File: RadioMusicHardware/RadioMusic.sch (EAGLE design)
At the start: 23 parts, among them IC1 TL074P, IC2 7805L, U1 USD-SOCKETNEW

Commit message: Output circuitry
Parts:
- added C3, C6: 1n, TomW:C-EU050-024X044
- added C7, C8: 100n, TomW:C-EU050-025X075
- added R3, R5, R6: 8.2k, TomW:R-EU_STANDARD_RESISTOR
- added R4: 220R, TomW:R-EU_STANDARD_RESISTOR
- added R7: 1k, TomW:R-EU_STANDARD_RESISTOR
- added R8: 3.3K, TomW:R-EU_STANDARD_RESISTOR
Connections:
- new net DAC: C8.2, U$1.RESET
- new net N$10: C8.1, R5.1
- new net N$2: C6.1, IC1C.+IN, R3.2
- new net N$4: C3.2, R3.1, R5.2
- new net N$5: C3.1, C7.2, IC1C.-IN, IC1C.OUT
- new net N$6: C7.1, IC1D.+IN, R6.2
- new net N$7: IC1D.-IN, R7.2, R8.1
- new net N$8: IC1D.OUT, R4.1, R8.2
- new net N$9: OUT1.3, R4.2
- net GND: now also C6.2, OUT1.5, R6.1, R7.1
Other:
- note added: "NB Outline is for Teensy3 Teensy3.1 has DAC output where Reset was on Teensy3"
- moved on the sheet: IC1C, IC1D, OUT1, OUT2, U1
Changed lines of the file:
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@@
 <layer number="97" name="Info" color="7" fill="1" visible="yes" active="yes"/>
 <layer number="98" name="Guide" color="6" fill="1" visible="yes" active="yes"/>
+<layer number="99" name="SpiceOrder" color="5" fill="1" visible="yes" active="yes"/>
 <layer number="100" name="Muster" color="7" fill="1" visible="no" active="no"/>
 <layer number="101" name="Patch_Top" color="12" fill="4" visible="yes" active="yes"/>
@@
 <part name="SUPPLY3" library="supply2" deviceset="GND" device=""/>
 <part name="SUPPLY4" library="supply2" deviceset="GND" device=""/>
+<part name="SUPPLY5" library="supply2" deviceset="GND" device=""/>
+<part name="R3" library="TomW" deviceset="R-EU_" device="STANDARD_RESISTOR" value="8.2k"/>
+<part name="R4" library="TomW" deviceset="R-EU_" device="STANDARD_RESISTOR" value="220R"/>
+<part name="R5" library="TomW" deviceset="R-EU_" device="STANDARD_RESISTOR" value="8.2k"/>
+<part name="C3" library="TomW" deviceset="C-EU" device="050-024X044" value="1n"/>
+<part name="C6" library="TomW" deviceset="C-EU" device="050-024X044" value="1n"/>
+<part name="SUPPLY6" library="supply2" deviceset="GND" device=""/>
+<part name="C7" library="TomW" deviceset="C-EU" device="050-025X075" value="100n"/>
+<part name="R6" library="TomW" deviceset="R-EU_" device="STANDARD_RESISTOR" value="8.2k"/>
+<part name="SUPPLY7" library="supply2" deviceset="GND" device=""/>
+<part name="R7" library="TomW" deviceset="R-EU_" device="STANDARD_RESISTOR" value="1k"/>
+<part name="SUPPLY8" library="supply2" deviceset="GND" device=""/>
+<part name="R8" library="TomW" deviceset="R-EU_" device="STANDARD_RESISTOR" value="3.3K"/>
+<part name="C8" library="TomW" deviceset="C-EU" device="050-025X075" value="100n"/>
 </parts>
 <sheets>
@@
 fuses with jumper wire.
 Don't get it the wrong way around! </text>
+<text x="104.14" y="142.24" size="0.762" layer="91">NB Outline is for Teensy3
+Teensy3.1 has DAC output
+where Reset was on Teensy3</text>
 </plain>
 <instances>
@@
 <instance part="CHANNEL_CV" gate="G$1" x="20.32" y="157.48" rot="MR0"/>
 <instance part="CV2" gate="G$1" x="17.78" y="93.98" rot="MR0"/>
-<instance part="OUT2" gate="G$1" x="233.68" y="124.46"/>
-<instance part="OUT1" gate="G$1" x="238.76" y="144.78"/>
+<instance part="OUT2" gate="G$1" x="-43.18" y="60.96"/>
+<instance part="OUT1" gate="G$1" x="269.24" y="66.04"/>
 <instance part="GAIN1" gate="G$1" x="17.78" y="71.12"/>
 <instance part="IC1" gate="A" x="66.04" y="157.48"/>
 <instance part="IC1" gate="B" x="66.04" y="88.9"/>
-<instance part="IC1" gate="C" x="190.5" y="116.84"/>
-<instance part="IC1" gate="D" x="185.42" y="142.24"/>
+<instance part="IC1" gate="C" x="182.88" y="71.12"/>
+<instance part="IC1" gate="D" x="231.14" y="68.58"/>
 <instance part="IC2" gate="A1" x="91.44" y="38.1"/>
-<instance part="U1" gate="G$1" x="274.32" y="119.38"/>
+<instance part="U1" gate="G$1" x="289.56" y="167.64"/>
 <instance part="R1" gate="G$1" x="45.72" y="160.02"/>
 <instance part="SUPPLY2" gate="GND" x="25.4" y="149.86"/>
@@
 <instance part="SUPPLY3" gate="GND" x="88.9" y="139.7"/>
 <instance part="SUPPLY4" gate="GND" x="20.32" y="116.84"/>
+<instance part="SUPPLY5" gate="GND" x="264.16" y="53.34"/>
+<instance part="R3" gate="G$1" x="162.56" y="73.66"/>
+<instance part="R4" gate="G$1" x="254" y="68.58"/>
+<instance part="R5" gate="G$1" x="142.24" y="73.66"/>
+<instance part="C3" gate="G$1" x="175.26" y="83.82" rot="R270"/>
+<instance part="C6" gate="G$1" x="170.18" y="58.42"/>
+<instance part="SUPPLY6" gate="GND" x="170.18" y="40.64"/>
+<instance part="C7" gate="G$1" x="205.74" y="71.12" rot="R270"/>
+<instance part="R6" gate="G$1" x="213.36" y="58.42" rot="R90"/>
+<instance part="SUPPLY7" gate="GND" x="213.36" y="38.1"/>
+<instance part="R7" gate="G$1" x="220.98" y="48.26" rot="R90"/>
+<instance part="SUPPLY8" gate="GND" x="220.98" y="38.1"/>
+<instance part="R8" gate="G$1" x="231.14" y="58.42"/>
+<instance part="C8" gate="G$1" x="129.54" y="73.66" rot="R270"/>
 </instances>
 <busses>
@@
 <pinref part="CHANNEL" gate="G$1" pin="A"/>
 <pinref part="SUPPLY4" gate="GND" pin="GND"/>
+</segment>
+<segment>
+<pinref part="OUT1" gate="G$1" pin="5"/>
+<pinref part="SUPPLY5" gate="GND" pin="GND"/>
+<wire x1="264.16" y1="55.88" x2="264.16" y2="63.5" width="0.1524" layer="91"/>
+</segment>
+<segment>
+<pinref part="C6" gate="G$1" pin="2"/>
+<pinref part="SUPPLY6" gate="GND" pin="GND"/>
+<wire x1="170.18" y1="53.34" x2="170.18" y2="43.18" width="0.1524" layer="91"/>
+</segment>
+<segment>
+<pinref part="R6" gate="G$1" pin="1"/>
+<pinref part="SUPPLY7" gate="GND" pin="GND"/>
+<wire x1="213.36" y1="40.64" x2="213.36" y2="53.34" width="0.1524" layer="91"/>
+</segment>
+<segment>
+<pinref part="R7" gate="G$1" pin="1"/>
+<pinref part="SUPPLY8" gate="GND" pin="GND"/>
+<wire x1="220.98" y1="40.64" x2="220.98" y2="43.18" width="0.1524" layer="91"/>
 </segment>
 </net>
@@
 </segment>
 </net>
+<net name="DAC" class="0">
+<segment>
+<pinref part="U$1" gate="G$1" pin="RESET"/>
+<wire x1="99.06" y1="137.16" x2="101.6" y2="137.16" width="0.1524" layer="91"/>
+<label x="99.06" y="137.16" size="1.778" layer="95" rot="R180" xref="yes"/>
+</segment>
+<segment>
+<pinref part="C8" gate="G$1" pin="2"/>
+<wire x1="119.38" y1="73.66" x2="124.46" y2="73.66" width="0.1524" layer="91"/>
+<label x="119.38" y="73.66" size="1.778" layer="95" rot="R180" xref="yes"/>
+</segment>
+</net>
+<net name="N$2" class="0">
+<segment>
+<pinref part="IC1" gate="C" pin="+IN"/>
+<pinref part="R3" gate="G$1" pin="2"/>
+<wire x1="167.64" y1="73.66" x2="170.18" y2="73.66" width="0.1524" layer="91"/>
+<pinref part="C6" gate="G$1" pin="1"/>
+<wire x1="170.18" y1="73.66" x2="175.26" y2="73.66" width="0.1524" layer="91"/>
+<wire x1="170.18" y1="60.96" x2="170.18" y2="73.66" width="0.1524" layer="91"/>
+<junction x="170.18" y="73.66"/>
+</segment>
+</net>
+<net name="N$4" class="0">
+<segment>
+<pinref part="R3" gate="G$1" pin="1"/>
+<pinref part="R5" gate="G$1" pin="2"/>
+<wire x1="147.32" y1="73.66" x2="152.4" y2="73.66" width="0.1524" layer="91"/>
+<pinref part="C3" gate="G$1" pin="2"/>
+<wire x1="152.4" y1="73.66" x2="157.48" y2="73.66" width="0.1524" layer="91"/>
+<wire x1="170.18" y1="83.82" x2="152.4" y2="83.82" width="0.1524" layer="91"/>
+<wire x1="152.4" y1="83.82" x2="152.4" y2="73.66" width="0.1524" layer="91"/>
+<junction x="152.4" y="73.66"/>
+</segment>
+</net>
+<net name="N$5" class="0">
+<segment>
+<pinref part="C3" gate="G$1" pin="1"/>
+<wire x1="177.8" y1="83.82" x2="195.58" y2="83.82" width="0.1524" layer="91"/>
+<wire x1="195.58" y1="83.82" x2="195.58" y2="71.12" width="0.1524" layer="91"/>
+<pinref part="IC1" gate="C" pin="OUT"/>
+<wire x1="195.58" y1="71.12" x2="190.5" y2="71.12" width="0.1524" layer="91"/>
+<pinref part="IC1" gate="C" pin="-IN"/>
+<wire x1="175.26" y1="68.58" x2="172.72" y2="68.58" width="0.1524" layer="91"/>
+<wire x1="172.72" y1="68.58" x2="172.72" y2="63.5" width="0.1524" layer="91"/>
+<wire x1="172.72" y1="63.5" x2="195.58" y2="63.5" width="0.1524" layer="91"/>
+<wire x1="195.58" y1="63.5" x2="195.58" y2="71.12" width="0.1524" layer="91"/>
+<junction x="195.58" y="71.12"/>
+<pinref part="C7" gate="G$1" pin="2"/>
+<wire x1="200.66" y1="71.12" x2="195.58" y2="71.12" width="0.1524" layer="91"/>
+</segment>
+</net>
+<net name="N$6" class="0">
+<segment>
+<pinref part="C7" gate="G$1" pin="1"/>
+<pinref part="IC1" gate="D" pin="+IN"/>
+<wire x1="208.28" y1="71.12" x2="213.36" y2="71.12" width="0.1524" layer="91"/>
+<wire x1="213.36" y1="71.12" x2="223.52" y2="71.12" width="0.1524" layer="91"/>
+<wire x1="213.36" y1="71.12" x2="213.36" y2="63.5" width="0.1524" layer="91"/>
+<junction x="213.36" y="71.12"/>
+<pinref part="R6" gate="G$1" pin="2"/>
+</segment>
+</net>
+<net name="N$7" class="0">
+<segment>
+<pinref part="IC1" gate="D" pin="-IN"/>
+<pinref part="R7" gate="G$1" pin="2"/>
+<wire x1="223.52" y1="66.04" x2="220.98" y2="66.04" width="0.1524" layer="91"/>
+<wire x1="220.98" y1="66.04" x2="220.98" y2="58.42" width="0.1524" layer="91"/>
+<pinref part="R8" gate="G$1" pin="1"/>
+<wire x1="220.98" y1="58.42" x2="220.98" y2="53.34" width="0.1524" layer="91"/>
+<wire x1="226.06" y1="58.42" x2="220.98" y2="58.42" width="0.1524" layer="91"/>
+<junction x="220.98" y="58.42"/>
+</segment>
+</net>
+<net name="N$8" class="0">
+<segment>
+<pinref part="IC1" gate="D" pin="OUT"/>
+<pinref part="R4" gate="G$1" pin="1"/>
+<wire x1="238.76" y1="68.58" x2="243.84" y2="68.58" width="0.1524" layer="91"/>
+<pinref part="R8" gate="G$1" pin="2"/>
+<wire x1="243.84" y1="68.58" x2="248.92" y2="68.58" width="0.1524" layer="91"/>
+<wire x1="236.22" y1="58.42" x2="243.84" y2="58.42" width="0.1524" layer="91"/>
+<wire x1="243.84" y1="58.42" x2="243.84" y2="68.58" width="0.1524" layer="91"/>
+<junction x="243.84" y="68.58"/>
+</segment>
+</net>
+<net name="N$9" class="0">
+<segment>
+<pinref part="R4" gate="G$1" pin="2"/>
+<pinref part="OUT1" gate="G$1" pin="3"/>
+<wire x1="264.16" y1="68.58" x2="259.08" y2="68.58" width="0.1524" layer="91"/>
+</segment>
+</net>
+<net name="N$10" class="0">
+<segment>
+<pinref part="R5" gate="G$1" pin="1"/>
+<pinref part="C8" gate="G$1" pin="1"/>
+<wire x1="132.08" y1="73.66" x2="137.16" y2="73.66" width="0.1524" layer="91"/>
+</segment>
+</net>

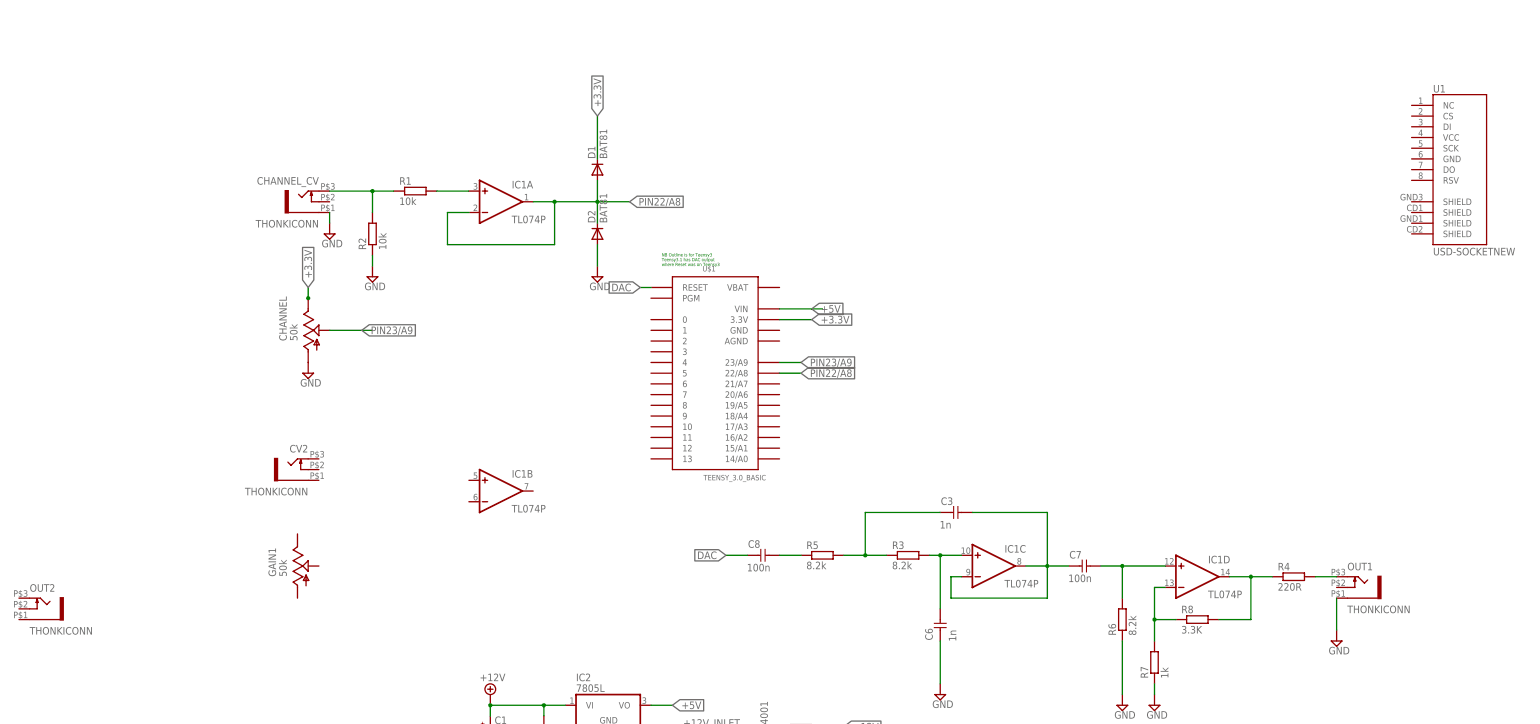
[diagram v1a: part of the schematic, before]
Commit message: Basic hardware schematic complete
Only needs SD connections & checking
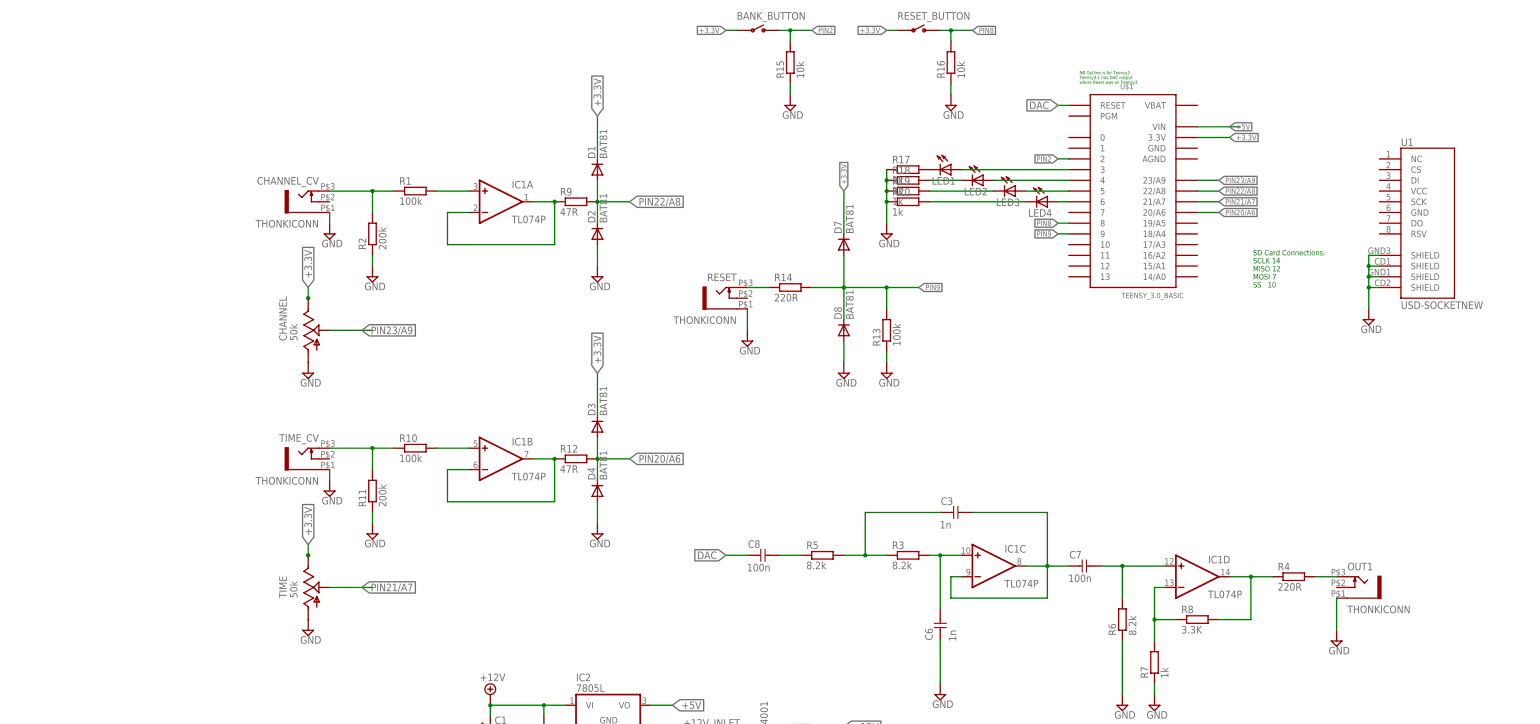
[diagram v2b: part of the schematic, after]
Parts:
- removed CV2, OUT2: THONKICONN, TomW:THONKICONN
- removed GAIN1: 50k, TomW:ALPHA-9MMF2A
- added BANK_BUTTON, RESET_BUTTON: D6_PUSH_SWITCH, TomW:D6_PUSH_SWITCH
- added D3, D4, D7, D8: BAT81, diode:BAT81
- added LED1, LED2, LED3, LED4: (no value), TomW:LED3MM
- added R10, R13: 100k, TomW:R-EU_STANDARD_RESISTOR
- added R11: 200k, TomW:R-EU_STANDARD_RESISTOR
- added R12, R9: 47R, TomW:R-EU_STANDARD_RESISTOR
- added R14: 220R, TomW:R-EU_STANDARD_RESISTOR
- added R15, R16: 10k, TomW:R-EU_STANDARD_RESISTOR
- added R17, R18, R19, R20: 1k, TomW:R-EU_STANDARD_RESISTOR
- added RESET, TIME_CV: THONKICONN, TomW:THONKICONN
- added TIME: 50k, TomW:ALPHA-9MMF2A
- R1: value 10k -> 100k
- R2: value 10k -> 200k
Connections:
- new net N$11: R10.1, R11.2, TIME_CV.3
- new net N$12: IC1B.+IN, R10.2
- new net N$13: LED1.A, U$1.3
- new net N$14: R14.1, RESET.3
- new net N$15: LED2.A, U$1.4
- new net N$16: LED3.A, U$1.5
- new net N$17: LED4.A, U$1.6
- new net N$18: LED1.C, R17.2
- new net N$19: LED2.C, R18.2
- new net N$20: LED3.C, R19.2
- new net N$21: LED4.C, R20.2
- new net PIN2: BANK_BUTTON.O, R15.2, U$1.2
- new net PIN20/A6: D3.A, D4.C, R12.2, U$1.20/A6
- new net PIN21/A7: TIME.S, U$1.21/A7
- new net PIN8: R16.2, RESET_BUTTON.O, U$1.8
- new net PIN9: D7.A, D8.C, R13.2, R14.2, U$1.9
- net +3.3V: now also BANK_BUTTON.P, D3.C, D7.C, RESET_BUTTON.P, TIME.E
- net GND: now also D4.A, D8.A, R11.1, R13.1, R15.1, R16.1, R17.1, R18.1, R19.1, R20.1, RESET.5, TIME.A, TIME_CV.5, U1.SHIELD@1, U1.SHIELD@2, U1.SHIELD@3, U1.SHIELD@4
- net PIN22/A8: now also IC1B.-IN, IC1B.OUT, R12.1, R9.1, R9.2
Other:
- note added: "SD Card Connections: SCLK 14 MISO 12 MOSI 7 SS 10"
- moved on the sheet: IC1B, U$1, U1

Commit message: Starting PCB layout
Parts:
- removed U1: USD-SOCKETNEW, SparkFun-Connectors:USD-SOCKETNEW
- added L1, L2: BL01RN1A, inductors:BL01RN1A
- added U$3: VERT_SD_CARD, TomW:VERT_SD_CARD
- CHANNEL_CV, OUT1, RESET, TIME_CV: value THONKICONN -> WQP-PJ301M-12_JACK; device TomW:THONKICONN -> thonkiconn:WQP-PJ301M-12_JACK
- U$1: value TEENSY_3.0_BASIC -> TEENSY_3.1_TW; device Teensy3.0:TEENSY_3.0_BASIC -> TomW:TEENSY_3.1_TW
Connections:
- new net MISO: U$1.12, U$3.DO
- new net MOSI: U$1.7, U$3.DI
- new net N$22: 1.P$2, L1.1
- new net N$23: FUSE.P$2, L2.1
- new net SCLK: U$1.14/A0, U$3.SCK
- new net SS: U$1.10, U$3.CS
- net +12V: now also L1.2; no longer 1.P$2
- net +3.3V: now also U$3.VCC
- net -12V: now also L2.2; no longer FUSE.P$2
- net DAC: now also U$1.DAC; no longer U$1.RESET
- net GND: now also CHANNEL_CV.1, OUT1.1, RESET.1, TIME_CV.1, U$3.GND, U$3.SHIELD@1, U$3.SHIELD@2; no longer CHANNEL_CV.5, OUT1.5, RESET.5, TIME_CV.5, U1.SHIELD@1, U1.SHIELD@2, U1.SHIELD@3, U1.SHIELD@4
- net N$1: now also CHANNEL_CV.2; no longer CHANNEL_CV.3
- net N$11: now also TIME_CV.2; no longer TIME_CV.3
- net N$14: now also RESET.2; no longer RESET.3
- net N$9: now also OUT1.2; no longer OUT1.3
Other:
- note added: "Optional reverse polarity protection If not required, omit diodes and replace fuses with jumper wire. Don't get it the wrong way around! Ferrites: 81-BL01RN1A1D2B or 623-2743001112LF"
- note removed: "Optional reverse polarity protection If not required, omit diodes and replace fuses with jumper wire. Don't get it the wrong way around!"
- moved on the sheet: LED1, LED4, R17, R18, R19, R20

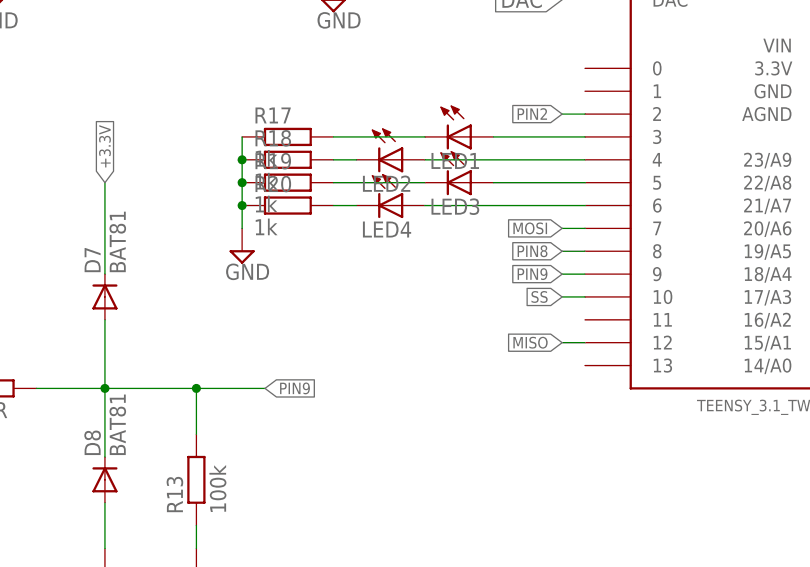
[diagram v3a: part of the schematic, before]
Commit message: Added collateral folder
Replace these files in the Teensy Audio Library
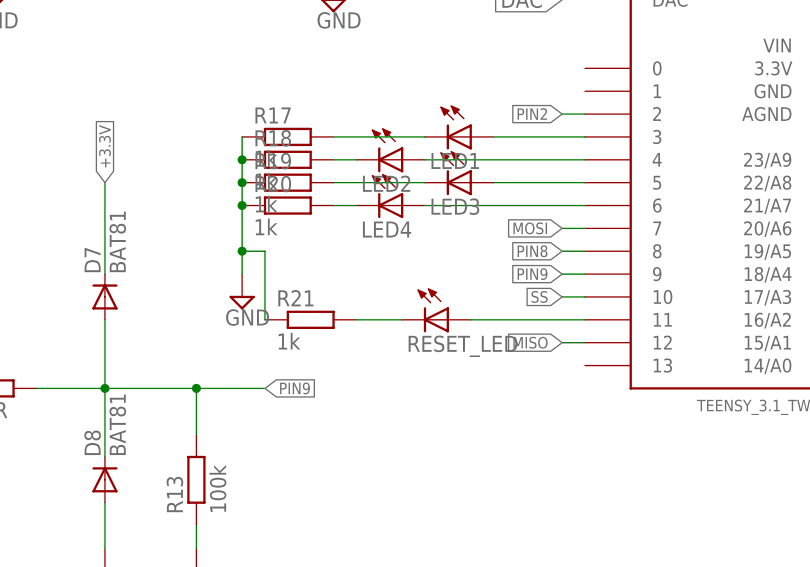
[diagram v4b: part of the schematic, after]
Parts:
- added R21: 1k, TomW:R-EU_STANDARD_RESISTOR
- added RESET_LED: (no value), TomW:LED3MM
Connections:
- new net N$24: RESET_LED.A, U$1.11
- new net N$25: R21.2, RESET_LED.C
- net GND: now also R21.1
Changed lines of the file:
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@@
 <part name="L1" library="inductors" deviceset="BL0" device="1RN1A"/>
 <part name="L2" library="inductors" deviceset="BL0" device="1RN1A"/>
+<part name="RESET_LED" library="TomW" deviceset="LED" device="3MM"/>
+<part name="R21" library="TomW" deviceset="R-EU_" device="STANDARD_RESISTOR" value="1k"/>
 </parts>
 <sheets>
@@
 <instance part="LED3" gate="G$1" x="187.96" y="160.02" rot="R270"/>
 <instance part="LED4" gate="G$1" x="180.34" y="157.48" rot="R270"/>
-<instance part="SUPPLY21" gate="GND" x="162.56" y="152.4"/>
+<instance part="SUPPLY21" gate="GND" x="162.56" y="147.32"/>
 <instance part="R17" gate="G$1" x="167.64" y="165.1"/>
 <instance part="R18" gate="G$1" x="167.64" y="162.56"/>
@@
 <instance part="L1" gate="G$1" x="149.86" y="33.02"/>
 <instance part="L2" gate="G$1" x="149.86" y="10.16"/>
+<instance part="RESET_LED" gate="G$1" x="185.42" y="144.78" rot="R270"/>
+<instance part="R21" gate="G$1" x="170.18" y="144.78"/>
 </instances>
 <busses>
@@
 <junction x="162.56" y="160.02"/>
 <pinref part="R20" gate="G$1" pin="1"/>
-<wire x1="162.56" y1="157.48" x2="162.56" y2="154.94" width="0.1524" layer="91"/>
+<wire x1="162.56" y1="157.48" x2="162.56" y2="152.4" width="0.1524" layer="91"/>
 <junction x="162.56" y="157.48"/>
+<pinref part="R21" gate="G$1" pin="1"/>
+<wire x1="162.56" y1="152.4" x2="162.56" y2="149.86" width="0.1524" layer="91"/>
+<wire x1="165.1" y1="144.78" x2="165.1" y2="152.4" width="0.1524" layer="91"/>
+<wire x1="165.1" y1="152.4" x2="162.56" y2="152.4" width="0.1524" layer="91"/>
+<junction x="162.56" y="152.4"/>
 </segment>
 <segment>
@@
 </segment>
 </net>
+<net name="N$24" class="0">
+<segment>
+<pinref part="U$1" gate="G$1" pin="11"/>
+<pinref part="RESET_LED" gate="G$1" pin="A"/>
+<wire x1="187.96" y1="144.78" x2="200.66" y2="144.78" width="0.1524" layer="91"/>
+</segment>
+</net>
+<net name="N$25" class="0">
+<segment>
+<pinref part="RESET_LED" gate="G$1" pin="C"/>
+<pinref part="R21" gate="G$1" pin="2"/>
+<wire x1="175.26" y1="144.78" x2="180.34" y2="144.78" width="0.1524" layer="91"/>
+</segment>
+</net>
